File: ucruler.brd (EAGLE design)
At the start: 200 x 32 mm, 49 parts

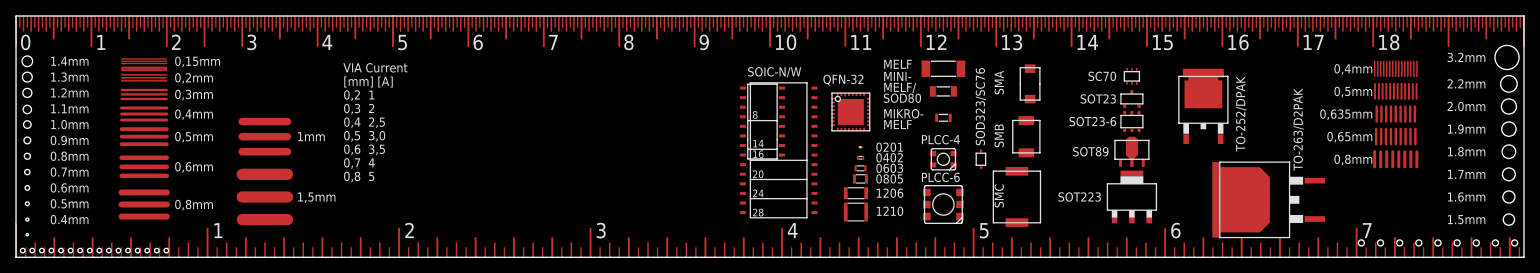
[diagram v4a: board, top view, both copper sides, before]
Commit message: reworked copper strips
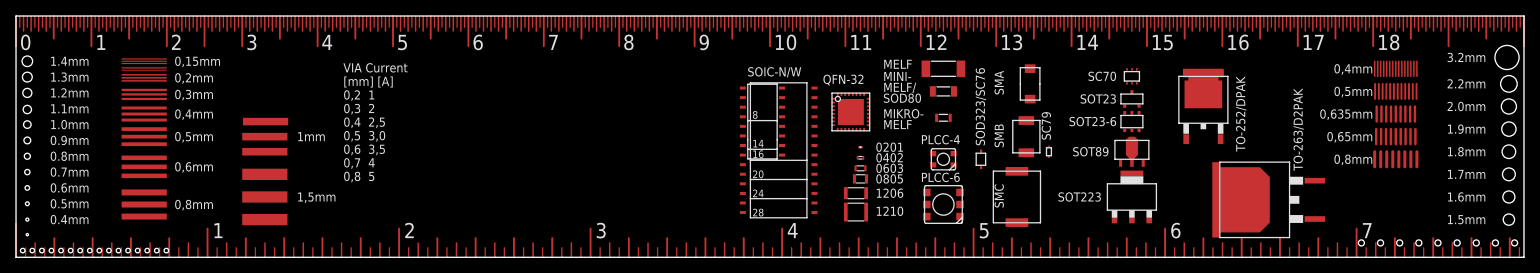
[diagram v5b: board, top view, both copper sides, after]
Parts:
- added E$50: (no value), ucruler:PACK-SC79
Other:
- board text added: "SC79"
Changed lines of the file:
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@@
 <text x="37.25" y="16" size="1.2" layer="21" rot="R180" align="center-right">1mm</text>
 <text x="37.25" y="8" size="1.2" layer="21" rot="R180" align="center-right">1,5mm</text>
-<rectangle x1="29" y1="4" x2="37" y2="19" layer="29"/>
-<rectangle x1="13.25" y1="4" x2="20.75" y2="27" layer="29"/>
+<rectangle x1="29.5" y1="4" x2="36.5" y2="19" layer="29"/>
+<rectangle x1="13.5" y1="4" x2="20.5" y2="27" layer="29"/>
 <text x="194.75" y="3" size="1.5" layer="22" rot="MR90" align="top-left">Owner</text>
 <hole x="198.755" y="1.905" drill="0.8"/>
@@
 <text x="107" y="23" size="1.2" layer="21" ratio="10" distance="20">QFN-32</text>
 <text x="128.5" y="14.75" size="1.2" layer="21" ratio="10" distance="20" rot="R90">SOD323/SC76</text>
+<text x="137.25" y="15.5" size="1.2" layer="21" ratio="10" distance="20" rot="R90">SC79</text>
 </plain>
 <attributes>
@@
 <element name="E$48" library="ucruler" package="PACK-QFN-32" value="" x="109" y="21"/>
 <element name="E$49" library="ucruler" package="PACK-SOD323" value="" x="128" y="13"/>
+<element name="E$50" library="ucruler" package="PACK-SC79" value="" x="137" y="14"/>
 </elements>
 <signals>

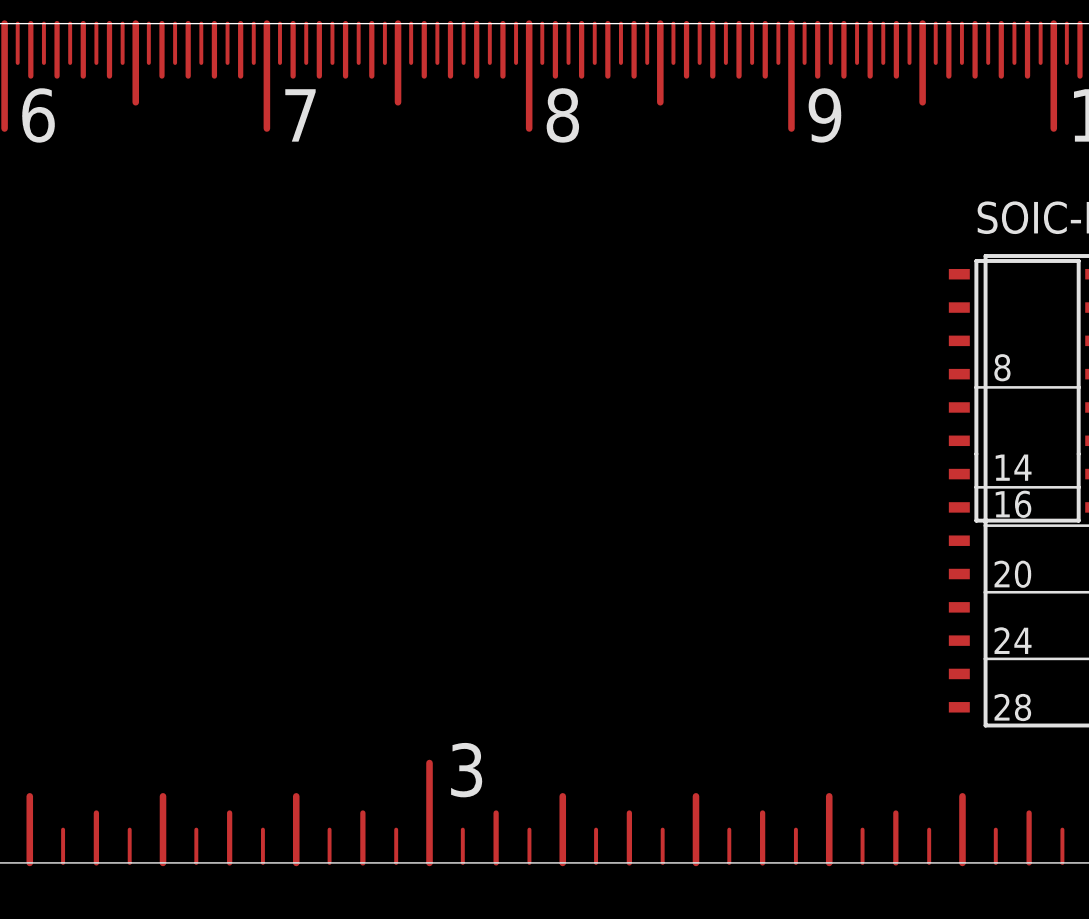
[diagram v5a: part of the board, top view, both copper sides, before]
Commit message: + smd electrolytic cap up to size F
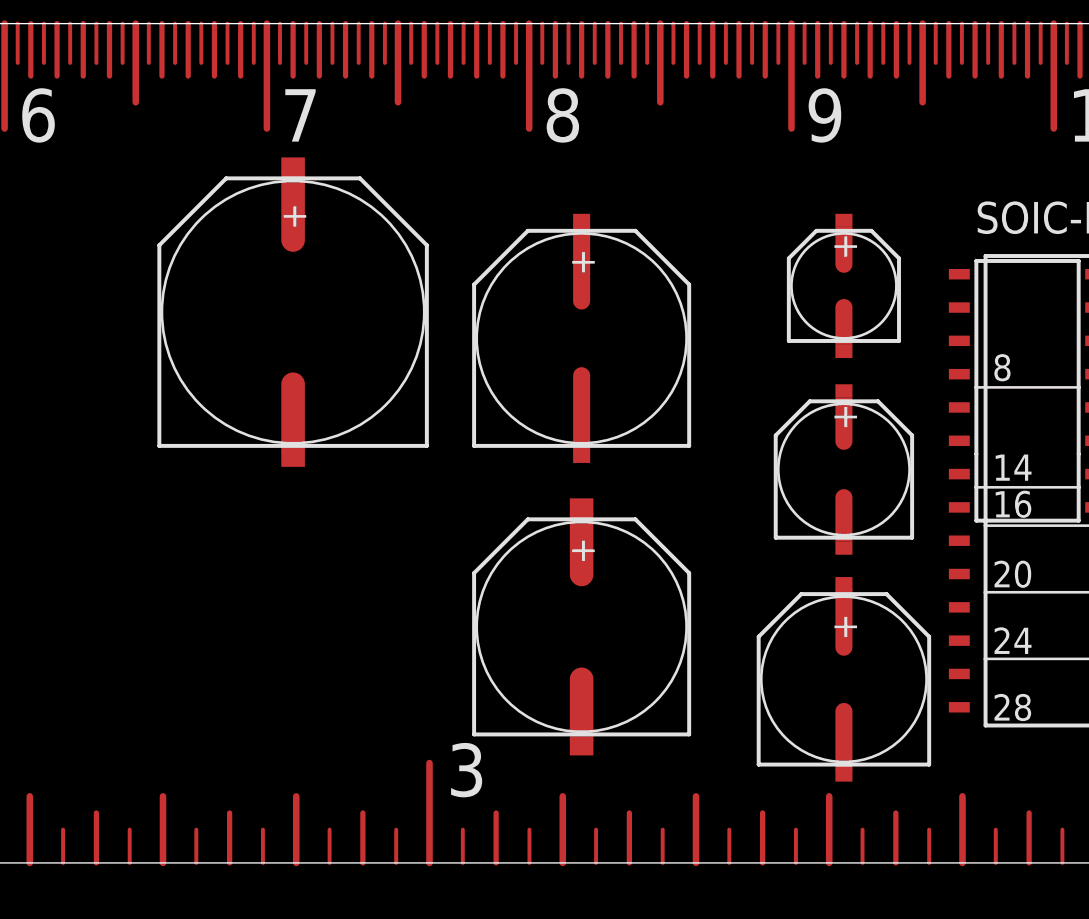
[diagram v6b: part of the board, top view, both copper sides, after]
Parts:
- added E$51: (no value), ucruler:PACK-ECAP-4.3
- added E$52: (no value), ucruler:PACK-ECAP-5.3
- added E$53: (no value), ucruler:PACK-ECAP-6.6
- added E$54: (no value), ucruler:PACK-ECAP-8.3-E
- added E$55: (no value), ucruler:PACK-ECAP-8.3-F
- added E$56: (no value), ucruler:PACK-ECAP-10.3
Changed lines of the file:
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@@
 <layer number="14" name="Route14" color="1" fill="6" visible="no" active="no"/>
 <layer number="15" name="Route15" color="4" fill="6" visible="no" active="no"/>
-<layer number="16" name="Bottom" color="1" fill="1" visible="yes" active="yes"/>
+<layer number="16" name="Bottom" color="1" fill="1" visible="no" active="no"/>
 <layer number="17" name="Pads" color="2" fill="1" visible="yes" active="yes"/>
 <layer number="18" name="Vias" color="2" fill="1" visible="yes" active="yes"/>
@@
 <layer number="27" name="tValues" color="7" fill="1" visible="yes" active="yes"/>
 <layer number="28" name="bValues" color="7" fill="1" visible="no" active="yes"/>
-<layer number="29" name="tStop" color="7" fill="3" visible="yes" active="yes"/>
+<layer number="29" name="tStop" color="7" fill="3" visible="no" active="yes"/>
 <layer number="30" name="bStop" color="7" fill="6" visible="no" active="yes"/>
 <layer number="31" name="tCream" color="7" fill="4" visible="no" active="yes"/>
@@
 <layer number="43" name="vRestrict" color="2" fill="10" visible="no" active="yes"/>
 <layer number="44" name="Drills" color="7" fill="1" visible="yes" active="yes"/>
-<layer number="45" name="Holes" color="7" fill="1" visible="yes" active="yes"/>
+<layer number="45" name="Holes" color="7" fill="1" visible="no" active="yes"/>
 <layer number="46" name="Milling" color="3" fill="1" visible="yes" active="yes"/>
-<layer number="47" name="Measures" color="7" fill="1" visible="yes" active="yes"/>
+<layer number="47" name="Measures" color="7" fill="1" visible="no" active="yes"/>
 <layer number="48" name="Document" color="7" fill="1" visible="no" active="yes"/>
 <layer number="49" name="Reference" color="7" fill="1" visible="no" active="yes"/>
@@
 </class>
 </classes>
-<designrules name="default">
+<designrules name="default *">
 <description language="de">&lt;b&gt;EAGLE Design-Regeln&lt;/b&gt;
 &lt;p&gt;
@@
 einem neuen Namen ab.
 </description>
-<param name="layerSetup" value="(1*16)"/>
-<param name="mtCopper" value="0.035mm 0.035mm 0.035mm 0.035mm 0.035mm 0.035mm 0.035mm 0.035mm 0.035mm 0.035mm 0.035mm 0.035mm 0.035mm 0.035mm 0.035mm 0.035mm"/>
+<param name="layerSetup" value="1"/>
+<param name="mtCopper" value="0.035mm 0.035mm 0.035mm 0.035mm 0.035mm 0.035mm 0.035mm 0.035mm 0.035mm 0.035mm 0.035mm 0.035mm 0.035mm 0.035mm 0.035mm 0mil"/>
 <param name="mtIsolate" value="1.5mm 0.15mm 0.2mm 0.15mm 0.2mm 0.15mm 0.2mm 0.15mm 0.2mm 0.15mm 0.2mm 0.15mm 0.2mm 0.15mm 0.2mm"/>
 <param name="mdWireWire" value="8mil"/>
@@
 <element name="E$49" library="ucruler" package="PACK-SOD323" value="" x="128" y="13"/>
 <element name="E$50" library="ucruler" package="PACK-SC79" value="" x="137" y="14"/>
+<element name="E$51" library="ucruler" package="PACK-ECAP-4.3" value="" x="92" y="22"/>
+<element name="E$52" library="ucruler" package="PACK-ECAP-5.3" value="" x="92" y="15"/>
+<element name="E$53" library="ucruler" package="PACK-ECAP-6.6" value="" x="92" y="7"/>
+<element name="E$54" library="ucruler" package="PACK-ECAP-8.3-E" value="" x="82" y="20"/>
+<element name="E$55" library="ucruler" package="PACK-ECAP-8.3-F" value="" x="82" y="9"/>
+<element name="E$56" library="ucruler" package="PACK-ECAP-10.3" value="" x="71" y="21"/>
 </elements>
 <signals>

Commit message: +ssop
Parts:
- added E$57: (no value), ucruler:PACK-SSOP
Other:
- board text added: "SSOP"
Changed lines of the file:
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@@
 <text x="128.5" y="14.75" size="1.2" layer="21" ratio="10" distance="20" rot="R90">SOD323/SC76</text>
 <text x="137.25" y="15.5" size="1.2" layer="21" ratio="10" distance="20" rot="R90">SC79</text>
+<text x="68" y="12" size="1.2" layer="21" ratio="10" distance="20">SSOP</text>
 </plain>
 <attributes>
@@
 <element name="E$55" library="ucruler" package="PACK-ECAP-8.3-F" value="" x="82" y="9"/>
 <element name="E$56" library="ucruler" package="PACK-ECAP-10.3" value="" x="71" y="21"/>
+<element name="E$57" library="ucruler" package="PACK-SSOP" value="" x="70" y="9"/>
 </elements>
 <signals>

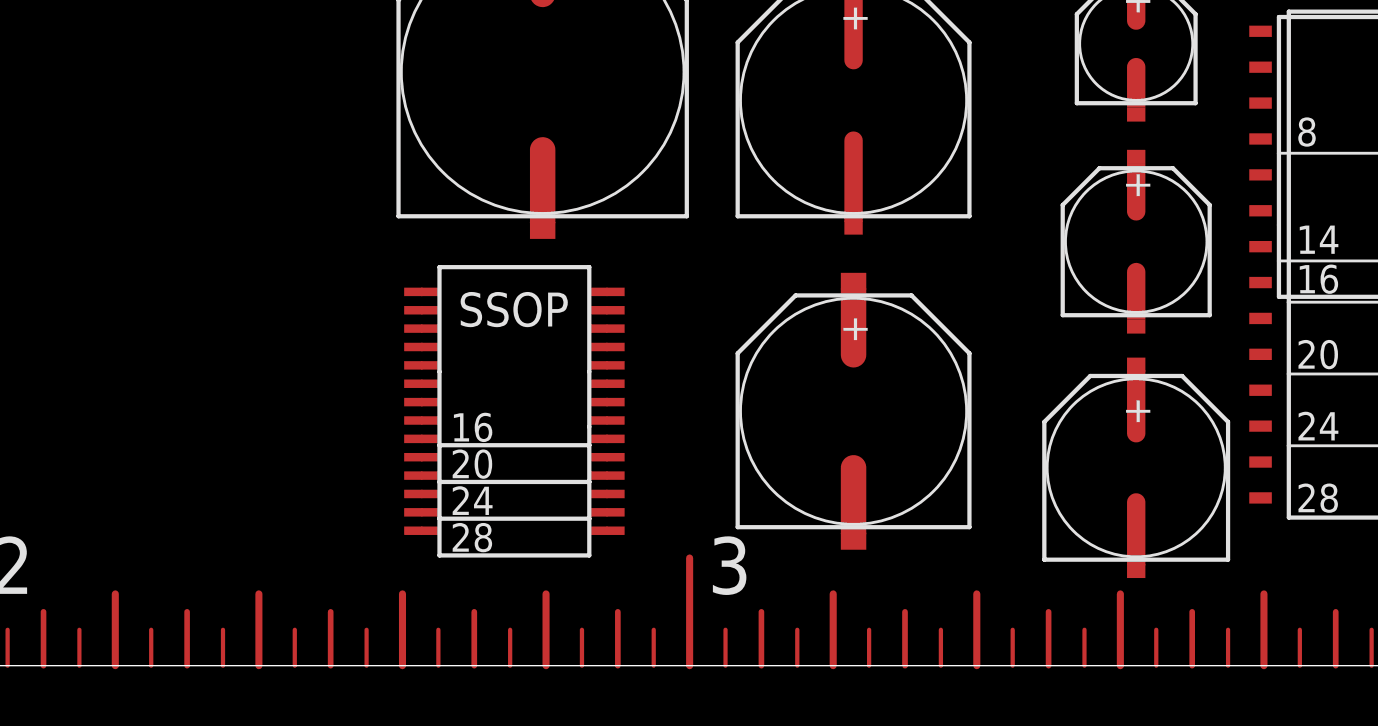
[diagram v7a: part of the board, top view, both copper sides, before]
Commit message: +tssop
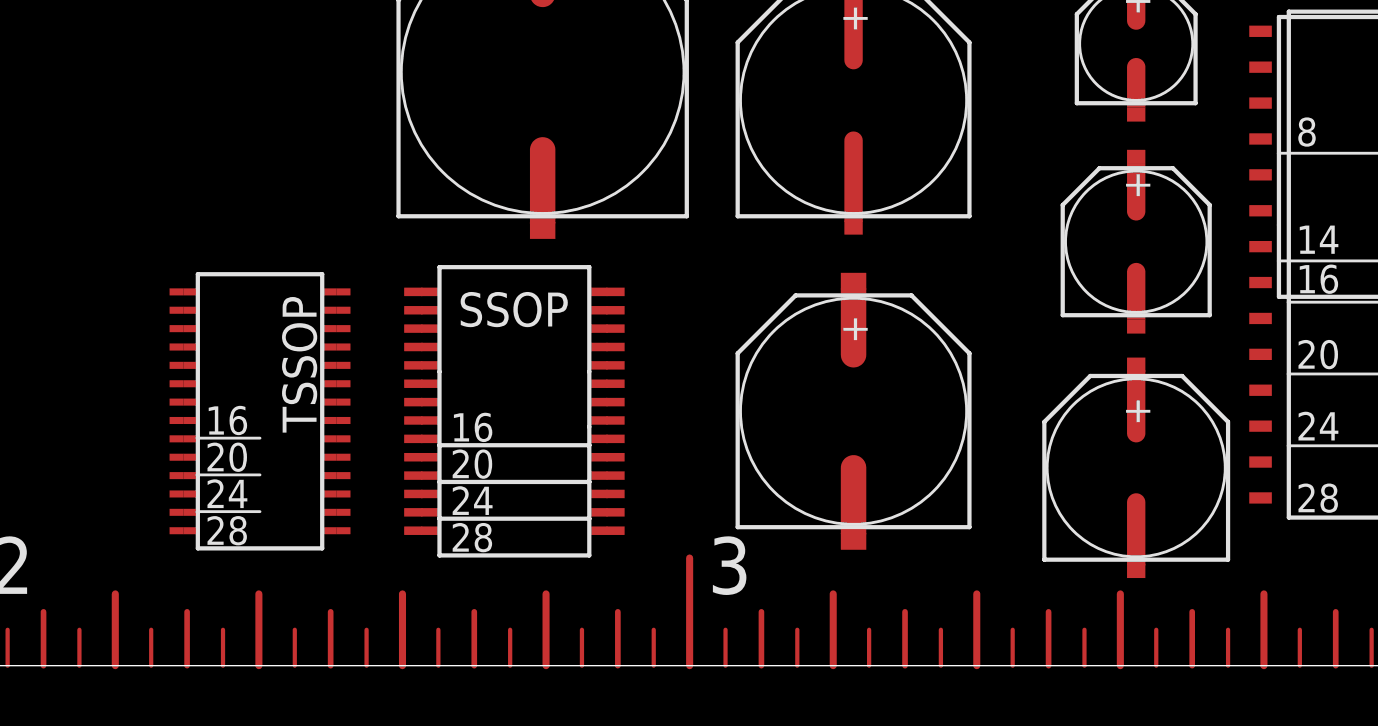
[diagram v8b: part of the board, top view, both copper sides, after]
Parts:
- added E$58: (no value), ucruler:PACK-TSSOP
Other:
- board text added: "TSSOP"
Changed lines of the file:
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@@
 <text x="137.25" y="15.5" size="1.2" layer="21" ratio="10" distance="20" rot="R90">SC79</text>
 <text x="68" y="12" size="1.2" layer="21" ratio="10" distance="20">SSOP</text>
+<text x="63" y="8.25" size="1.2" layer="21" ratio="10" distance="20" rot="R90">TSSOP</text>
 </plain>
 <attributes>
@@
 <element name="E$56" library="ucruler" package="PACK-ECAP-10.3" value="" x="71" y="21"/>
 <element name="E$57" library="ucruler" package="PACK-SSOP" value="" x="70" y="9"/>
+<element name="E$58" library="ucruler" package="PACK-TSSOP" value="" x="61" y="9"/>
 </elements>
 <signals>
